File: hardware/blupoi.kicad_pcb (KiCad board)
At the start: 2 copper layers, 229.7 x 29.5 mm, 135 parts, among them P1 MICRO-B-USB, SW1 PM_BTN, U1 NRF52832, U2 TPS63031DSKR, U3 bno055, U4 ics43432, U5 BQ24075RGTT, U6 MAX16054AZT+T, U7 sip32408, X1 32MHz

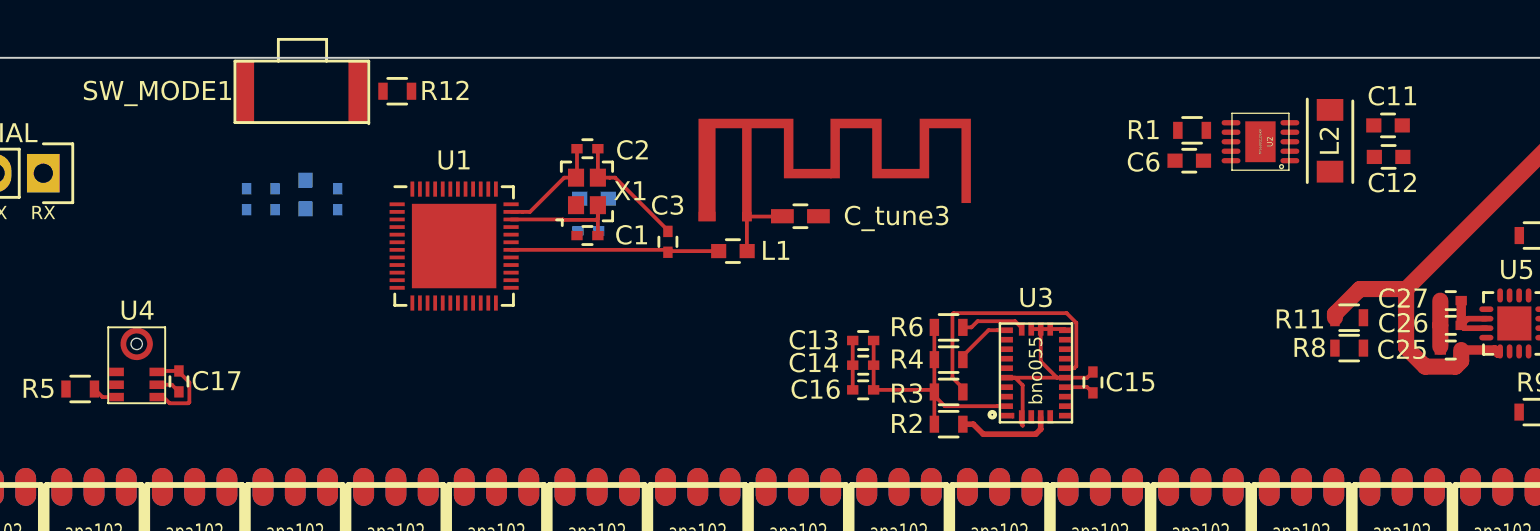
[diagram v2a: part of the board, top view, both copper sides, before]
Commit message: Change net name from VCHG to VREG
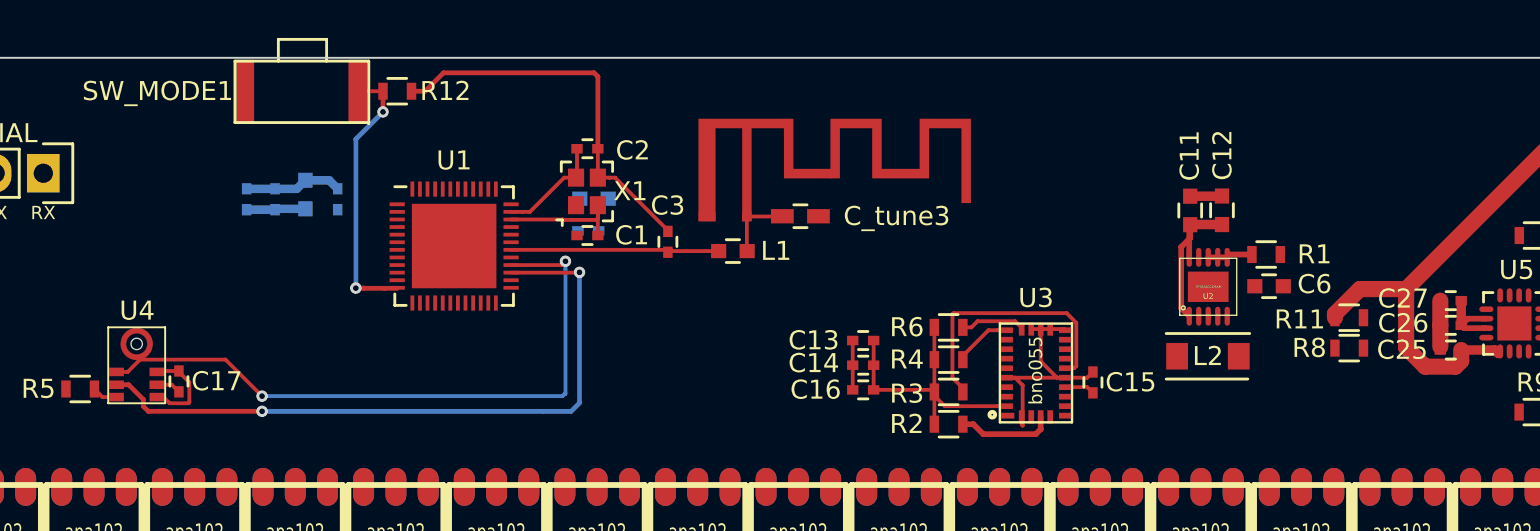
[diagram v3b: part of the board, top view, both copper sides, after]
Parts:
- moved L2 13.0 mm to (53.3, 108.8), turned to 180 degrees
- moved C11 11.3 mm to (52.4, 101.2), turned to 90 degrees
- moved C12 9.21 mm to (54.1, 101.2), turned to 90 degrees
- moved U2 8.12 mm to (53.4, 105.2), turned to 0 degrees
- moved C6 7.83 mm to (56.6, 105.2), turned to 180 degrees
- moved R1 7.61 mm to (56.4, 103.5), turned to 0 degrees
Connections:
- net VCHG renamed VREG
- U2 pad 2: Net-(U2-Pad2) -> Net-(L2-Pad2)
- U2 pad 4: Net-(U2-Pad4) -> Net-(L2-Pad1)
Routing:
- net MIC_I2S_SCK: track 0.00 -> 35.9 mm, vias 0 -> 2
- net MIC_I2S_WS: track 0.00 -> 34.7 mm, vias 0 -> 2
- net GND: track 78.9 -> 99.8 mm
- net Net-(R12-Pad1): track 0.00 -> 14.5 mm, vias 0 -> 2
- net V3.3: track 19.7 -> 31.4 mm
- net Net-(R1-Pad1): track 0.00 -> 2.36 mm

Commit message: Fixed SIP32408 footprint pins/pads lacking GND
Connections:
- U7 pad 2: Net-(U7-Pad2) -> GND
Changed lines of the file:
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@@
 (kicad_pcb (version 20170123) (host pcbnew no-vcs-found-7663~57~ubuntu16.10.1)
   (general
-    (links 514)
-    (no_connects 414)
+    (links 515)
+    (no_connects 415)
     (area -60.860001 93.069999 168.980001 122.650001)
     (thickness 1.6)
@@
     (zones 0)
     (modules 135)
-    (nets 233)
+    (nets 232)
   )
   (page A4)
@@
   (net 228 "Net-(U6-Pad5)")
   (net 229 "Net-(U1-Pad11)")
-  (net 230 "Net-(U7-Pad2)")
-  (net 231 "Net-(R12-Pad1)")
-  (net 232 VREG)
+  (net 230 "Net-(R12-Pad1)")
+  (net 231 VREG)
   (net_class Default "This is the default net class."
     (clearance 0.2)
@@
     (add_net "Net-(U6-Pad4)")
     (add_net "Net-(U6-Pad5)")
-    (add_net "Net-(U7-Pad2)")
     (add_net PM_!CHG)
     (add_net PM_!GOOD)
@@
     (add_net VUSB)
   )
+  (module sip32408:sip32408 (layer F.Cu)
+    (at 81.22 107.89 270)
+    (fp_text reference U7 (at -2.065 0.915) (layer F.SilkS)
+      (effects (font (size 1 1) (thickness 0.15)))
+    )
+    (fp_text value sip32408 (at 0 -2.54 270) (layer F.Fab)
+      (effects (font (size 1 1) (thickness 0.15)))
+    )
+    (fp_text user . (at 0.23 1.5 270) (layer F.SilkS)
+      (effects (font (size 1 1) (thickness 0.15)))
+    )
+    (fp_line (start -1.27 1.65) (end -1.27 0) (layer F.SilkS) (width 0.15))
+    (fp_line (start -0.02 1.65) (end -1.27 1.65) (layer F.SilkS) (width 0.15))
+    (fp_line (start -0.02 0) (end -0.02 1.65) (layer F.SilkS) (width 0.15))
+    (fp_line (start -1.27 0) (end -0.02 0) (layer F.SilkS) (width 0.15))
+    (pad 5 smd rect (at -0.645 0.825 270) (size 0.86 0.5) (layers F.Cu F.Paste F.Mask)
+      (net 2 GND))
+    (pad 3 smd rect (at -0.895 0 270) (size 0.3 0.7) (layers F.Cu F.Paste F.Mask)
+      (net 228 "Net-(U6-Pad5)"))
+    (pad 4 smd rect (at -0.395 0 270) (size 0.3 0.7) (layers F.Cu F.Paste F.Mask)
+      (net 184 VIN))
+    (pad 1 smd rect (at -0.395 1.65 270) (size 0.3 0.7) (layers F.Cu F.Paste F.Mask)
+      (net 231 VREG))
+    (pad 2 smd rect (at -0.895 1.65 270) (size 0.3 0.7) (layers F.Cu F.Paste F.Mask)
+      (net 2 GND))
+  )
   (module bno055:bno055 (layer F.Cu)
     (at 44.282 109.718 90)
@@
       (net 229 "Net-(U1-Pad11)"))
     (pad 12 smd rect (at -3 2.2) (size 0.8 0.2) (layers F.Cu F.Paste F.Mask)
-      (net 231 "Net-(R12-Pad1)") (clearance 0.001))
+      (net 230 "Net-(R12-Pad1)") (clearance 0.001))
     (pad 13 smd rect (at -2.2 3 90) (size 0.8 0.2) (layers F.Cu F.Paste F.Mask)
       (net 186 V3.3))
@@
     (fp_line (start -0.25 0.475) (end 0.25 0.475) (layer F.SilkS) (width 0.15))
     (pad 1 smd rect (at -0.55 0 180) (size 0.6 0.5) (layers F.Cu F.Paste F.Mask)
-      (net 232 VREG))
+      (net 231 VREG))
     (pad 2 smd rect (at 0.55 0 180) (size 0.6 0.5) (layers F.Cu F.Paste F.Mask)
       (net 2 GND))
@@
     (fp_line (start -0.25 0.475) (end 0.25 0.475) (layer F.SilkS) (width 0.15))
     (pad 1 smd rect (at -0.55 0 180) (size 0.6 0.5) (layers F.Cu F.Paste F.Mask)
-      (net 232 VREG))
+      (net 231 VREG))
     (pad 2 smd rect (at 0.55 0 180) (size 0.6 0.5) (layers F.Cu F.Paste F.Mask)
       (net 2 GND))
@@
       (net 201 PM_!CHG))
     (pad 10 smd oval (at 1.475 0.25 180) (size 0.75 0.3) (layers F.Cu F.Paste F.Mask)
-      (net 232 VREG))
+      (net 231 VREG))
     (pad 11 smd oval (at 1.475 -0.25 180) (size 0.75 0.3) (layers F.Cu F.Paste F.Mask)
-      (net 232 VREG))
+      (net 231 VREG))
     (pad 12 smd oval (at 1.475 -0.75 180) (size 0.75 0.3) (layers F.Cu F.Paste F.Mask)
       (net 188 "Net-(R8-Pad1)"))
@@
     )
   )
-  (module sip32408:sip32408 (layer F.Cu)
-    (at 81.22 107.89 270)
-    (fp_text reference U7 (at -2.065 0.915) (layer F.SilkS)
-      (effects (font (size 1 1) (thickness 0.15)))
-    )
-    (fp_text value sip32408 (at 0 -2.54 270) (layer F.Fab)
-      (effects (font (size 1 1) (thickness 0.15)))
-    )
-    (fp_line (start -1.27 0) (end -0.02 0) (layer F.SilkS) (width 0.15))
-    (fp_line (start -0.02 0) (end -0.02 1.65) (layer F.SilkS) (width 0.15))
-    (fp_line (start -0.02 1.65) (end -1.27 1.65) (layer F.SilkS) (width 0.15))
-    (fp_line (start -1.27 1.65) (end -1.27 0) (layer F.SilkS) (width 0.15))
-    (fp_text user . (at 0.23 1.5 270) (layer F.SilkS)
-      (effects (font (size 1 1) (thickness 0.15)))
-    )
-    (pad 2 smd rect (at -0.895 1.65 270) (size 0.3 0.7) (layers F.Cu F.Paste F.Mask)
-      (net 230 "Net-(U7-Pad2)"))
-    (pad 1 smd rect (at -0.395 1.65 270) (size 0.3 0.7) (layers F.Cu F.Paste F.Mask)
-      (net 232 VREG))
-    (pad 4 smd rect (at -0.395 0 270) (size 0.3 0.7) (layers F.Cu F.Paste F.Mask)
-      (net 184 VIN))
-    (pad 3 smd rect (at -0.895 0 270) (size 0.3 0.7) (layers F.Cu F.Paste F.Mask)
-      (net 228 "Net-(U6-Pad5)"))
-    (pad 1 smd rect (at -0.645 0.825 270) (size 0.86 0.5) (layers F.Cu F.Paste F.Mask)
-      (net 232 VREG))
-    (model ${KISYS3DMOD}/Housings_DFN_QFN.3dshapes/DFN-6-1EP_2x2mm_Pitch0.5mm.wrl
-      (at (xyz -0.02362204724409449 -0.03149606299212599 0))
-      (scale (xyz 0.75 0.75 0.75))
-      (rotate (xyz 0 0 90))
-    )
-  )
   (module Resistors_SMD:R_0603 (layer F.Cu)
     (at 10.64 94.88)
@@
       (net 2 GND))
     (pad 1 smd rect (at -0.75 0) (size 0.5 0.9) (layers F.Cu F.Paste F.Mask)
-      (net 231 "Net-(R12-Pad1)"))
+      (net 230 "Net-(R12-Pad1)"))
     (model Resistors_SMD.3dshapes/R_0603.wrl
       (at (xyz 0 0 0))
@@
     (fp_line (start 0 -0.0635) (end 0 3.2385) (layer F.SilkS) (width 0.15))
     (pad 1 smd rect (at 0.5715 1.651 180) (size 1 3.3) (layers F.Cu F.Paste F.Mask)
-      (net 231 "Net-(R12-Pad1)"))
+      (net 230 "Net-(R12-Pad1)"))
     (pad 2 smd rect (at 6.5405 1.651 180) (size 1 3.3) (layers F.Cu F.Paste F.Mask)
       (net 186 V3.3))
@@
   (via (at 163 93.6) (size 0.6) (drill 0.3) (layers F.Cu B.Cu) (net 192))
   (segment (start -42.43 120.52) (end -42.43 120.07) (width 0.2) (layer B.Cu) (net 203))
-  (segment (start 8.46 105.25) (end 8.884264 105.25) (width 0.25) (layer F.Cu) (net 231))
-  (segment (start 8.884264 105.25) (end 8.893784 105.25952) (width 0.25) (layer F.Cu) (net 231))
-  (segment (start 8.893784 105.25952) (end 9.975999 105.25952) (width 0.25) (layer F.Cu) (net 231))
-  (segment (start 9.975999 105.25952) (end 10.636 105.25952) (width 0.25) (layer F.Cu) (net 231))
-  (via (at 8.46 105.25) (size 0.6) (drill 0.3) (layers F.Cu B.Cu) (net 231))
-  (segment (start 8.46 97.4) (end 8.46 105.25) (width 0.25) (layer B.Cu) (net 231))
-  (segment (start 9.89 95.97) (end 8.46 97.4) (width 0.25) (layer B.Cu) (net 231))
-  (segment (start 9.89 94.88) (end 9.89 95.97) (width 0.25) (layer F.Cu) (net 231))
-  (via (at 9.89 95.97) (size 0.6) (drill 0.3) (layers F.Cu B.Cu) (net 231))
-  (segment (start 8.57 94.88) (end 9.89 94.88) (width 0.2) (layer F.Cu) (net 231))
-  (segment (start 66.68 105.91) (end 66.68 107.21) (width 0.5) (layer F.Cu) (net 232))
-  (segment (start 68.005 106.86) (end 67.03 106.86) (width 0.3) (layer F.Cu) (net 232))
-  (segment (start 67.03 106.86) (end 66.68 107.21) (width 0.3) (layer F.Cu) (net 232))
-  (segment (start 68.005 107.36) (end 66.83 107.36) (width 0.3) (layer F.Cu) (net 232))
-  (segment (start 66.83 107.36) (end 66.68 107.21) (width 0.3) (layer F.Cu) (net 232))
+  (segment (start 8.46 105.25) (end 8.884264 105.25) (width 0.25) (layer F.Cu) (net 230))
+  (segment (start 8.884264 105.25) (end 8.893784 105.25952) (width 0.25) (layer F.Cu) (net 230))
+  (segment (start 8.893784 105.25952) (end 9.975999 105.25952) (width 0.25) (layer F.Cu) (net 230))
+  (segment (start 9.975999 105.25952) (end 10.636 105.25952) (width 0.25) (layer F.Cu) (net 230))
+  (via (at 8.46 105.25) (size 0.6) (drill 0.3) (layers F.Cu B.Cu) (net 230))
+  (segment (start 8.46 97.4) (end 8.46 105.25) (width 0.25) (layer B.Cu) (net 230))
+  (segment (start 9.89 95.97) (end 8.46 97.4) (width 0.25) (layer B.Cu) (net 230))
+  (segment (start 9.89 94.88) (end 9.89 95.97) (width 0.25) (layer F.Cu) (net 230))
+  (via (at 9.89 95.97) (size 0.6) (drill 0.3) (layers F.Cu B.Cu) (net 230))
+  (segment (start 8.57 94.88) (end 9.89 94.88) (width 0.2) (layer F.Cu) (net 230))
+  (segment (start 66.68 105.91) (end 66.68 107.21) (width 0.5) (layer F.Cu) (net 231))
+  (segment (start 68.005 106.86) (end 67.03 106.86) (width 0.3) (layer F.Cu) (net 231))
+  (segment (start 67.03 106.86) (end 66.68 107.21) (width 0.3) (layer F.Cu) (net 231))
+  (segment (start 68.005 107.36) (end 66.83 107.36) (width 0.3) (layer F.Cu) (net 231))
+  (segment (start 66.83 107.36) (end 66.68 107.21) (width 0.3) (layer F.Cu) (net 231))
   (zone (net 0) (net_name "") (layer F.Cu) (hatch edge 0.508)
     (connect_pads (clearance 0.508))

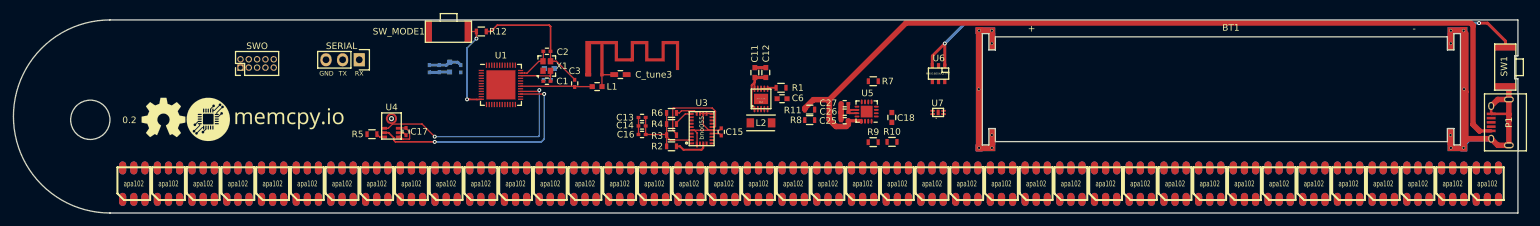
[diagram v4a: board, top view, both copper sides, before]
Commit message: Started routing v0.2
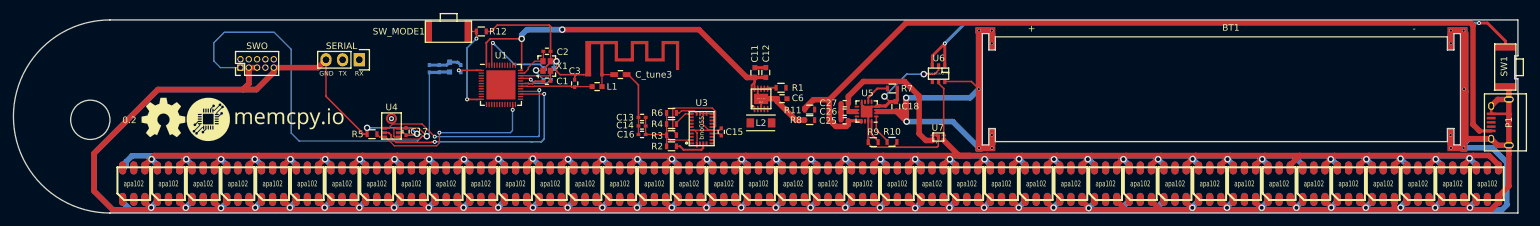
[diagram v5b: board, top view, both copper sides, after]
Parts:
- moved U7 3.76 mm to (81.2, 111.6)
- moved R7 3.12 mm to (73.4, 103.6)
- moved C18 1.78 mm to (73.9, 106.3), turned to 90 degrees
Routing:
- net GND: track 99.8 -> 946.7 mm, vias 0 -> 43
- net VIN: track 0.00 -> 613.4 mm, vias 0 -> 38
- net V3.3: track 31.4 -> 157.5 mm, vias 0 -> 3
- net VBAT: track 12.9 -> 61.4 mm, vias 0 -> 2
- net MIC_I2S_SD: track 1.33 -> 27.3 mm, vias 0 -> 2
- net VREG: track 4.16 -> 27.7 mm
- net Net-(C10-Pad1): track 0.00 -> 13.0 mm, vias 0 -> 1
- net Net-(U6-Pad5): track 0.00 -> 8.56 mm
- net Net-(C7-Pad1): track 0.00 -> 5.16 mm, vias 0 -> 1
- net Net-(R10-Pad1): track 0.00 -> 4.56 mm
- net PM_EN1: track 0.00 -> 4.17 mm
- net Net-(C4-Pad1): track 0.00 -> 3.87 mm, vias 0 -> 1
- net PM_ISET: track 0.00 -> 3.61 mm
- net Net-(C1-Pad1): track 6.90 -> 6.29 mm

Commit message: Started routing v0.2..
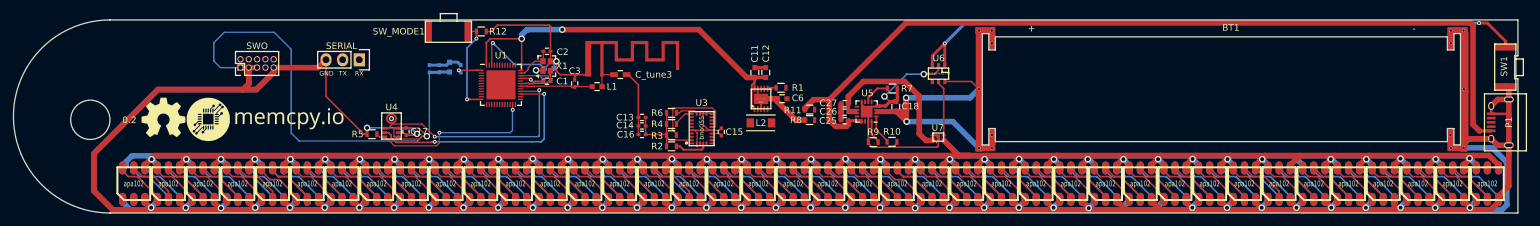
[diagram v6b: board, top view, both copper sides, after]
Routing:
- net Net-(LED0_4-Pad5): track 0.00 -> 8.02 mm
- net Net-(LED0_33-Pad5): track 0.00 -> 8.02 mm
- net Net-(LED0_16-Pad5): track 0.00 -> 8.02 mm
- net Net-(LED0_1-Pad5): track 0.00 -> 8.02 mm
- net Net-(LED1_39-Pad5): track 0.00 -> 7.82 mm
- net Net-(LED1_38-Pad5): track 0.00 -> 7.82 mm
- net Net-(LED1_36-Pad5): track 0.00 -> 7.82 mm
- net Net-(LED1_34-Pad5): track 0.00 -> 7.82 mm
- net Net-(LED1_31-Pad5): track 0.00 -> 7.82 mm
- net Net-(LED1_26-Pad5): track 0.00 -> 7.82 mm
- net Net-(LED0_38-Pad6): track 0.00 -> 7.82 mm
- net Net-(LED0_37-Pad6): track 0.00 -> 7.82 mm
- net Net-(LED0_35-Pad6): track 0.00 -> 7.82 mm
- net Net-(LED0_30-Pad6): track 0.00 -> 7.82 mm
- net Net-(LED0_25-Pad6): track 0.00 -> 7.82 mm
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
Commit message: Started routing v0.2...
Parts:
- moved SWO 38.8 mm to (11.2, 110.8)
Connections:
- LED1_1 pad 1: /apa102_1/SPI0_MOSI -> APA102_1_MOSI
- LED1_1 pad 2: /apa102_1/SPI0_SCK -> APA102_1_SCK
- U1 pad 10: Net-(U1-Pad10) -> MIC_I2S_SD
- U1 pad 23: MIC_I2S_SD -> Net-(U1-Pad23)
- U1 pad 27: MIC_I2S_SCK -> ACC_I2C_SCL
- U1 pad 28: MIC_I2S_WS -> ACC_I2C_SDA
- U1 pad 37: APA102_0_MOSI -> Net-(U1-Pad37)
- U1 pad 38: APA102_0_SCK -> Net-(U1-Pad38)
- U1 pad 39: APA102_1_MOSI -> Net-(U1-Pad39)
- U1 pad 4: Net-(U1-Pad4) -> APA102_0_SCK
- U1 pad 40: APA102_1_SCK -> Net-(U1-Pad40)
- U1 pad 5: Net-(U1-Pad5) -> APA102_0_MOSI
- U1 pad 6: Net-(U1-Pad6) -> APA102_1_SCK
- U1 pad 7: Net-(U1-Pad7) -> APA102_1_MOSI
- U1 pad 8: ACC_I2C_SCL -> MIC_I2S_WS
- U1 pad 9: ACC_I2C_SDA -> MIC_I2S_SCK
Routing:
- net APA102_0_SCK: track 0.00 -> 72.8 mm, vias 0 -> 2
- net APA102_0_MOSI: track 0.00 -> 72.8 mm, vias 0 -> 2
- net APA102_1_SCK: track 0.00 -> 70.7 mm, vias 0 -> 1
- net APA102_1_MOSI: track 0.00 -> 70.0 mm, vias 0 -> 1
- net V3.3: track 157.5 -> 123.1 mm, vias 3 -> 4
- net TX: track 0.00 -> 22.2 mm
- net RX: track 0.00 -> 19.5 mm
- net GND: track 946.7 -> 965.8 mm
- net VIN: track 613.4 -> 628.7 mm, vias 38 -> 40
- net MIC_I2S_SCK: track 35.9 -> 21.6 mm
- net MIC_I2S_WS: track 34.7 -> 21.7 mm
- net SWDIO: track 0.00 -> 11.5 mm, vias 0 -> 1
- net SWCLK: track 0.00 -> 9.48 mm, vias 0 -> 1
- net MIC_I2S_SD: track 27.3 -> 23.1 mm
- net SWO: track 0.00 -> 3.87 mm
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
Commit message: Finished routing for v0.2
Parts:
- moved SWO 1.37 mm to (11.1, 112.2)
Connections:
- U1 pad 15: PM_EN1 -> PM_!CHG
- U1 pad 16: PM_EN2 -> PM_!GOOD
- U1 pad 17: PM_!GOOD -> PM_EN1
- U1 pad 18: PM_!CHG -> PM_EN2
- U1 pad 27: ACC_I2C_SCL -> ACC_I2C_SDA
- U1 pad 28: ACC_I2C_SDA -> ACC_I2C_SCL
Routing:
- net GND: track 965.8 -> 1107.7 mm, vias 43 -> 54
- net PM_SWITCH: track 96.6 -> 166.1 mm, vias 2 -> 4
- net PM_EN2: track 0.00 -> 68.1 mm, vias 0 -> 4
- net PM_ISET: track 3.61 -> 70.2 mm, vias 0 -> 2
- net PM_!CHG: track 0.00 -> 64.9 mm, vias 0 -> 2
- net PM_!GOOD: track 0.00 -> 64.8 mm, vias 0 -> 2
- net PM_EN1: track 4.17 -> 68.5 mm, vias 0 -> 2
- net V3.3: track 123.1 -> 153.0 mm, vias 4 -> 9
- net ACC_I2C_SDA: track 5.07 -> 29.6 mm, vias 1 -> 0
- net ACC_I2C_SCL: track 5.64 -> 29.0 mm, vias 1 -> 0
- net Net-(R8-Pad1): track 0.00 -> 10.2 mm, vias 0 -> 2
- net Net-(R3-Pad1): track 14.0 -> 9.31 mm, vias 0 -> 2
- net SWDIO: track 11.5 -> 14.8 mm
- net VUSB: track 136.0 -> 137.6 mm
- net SWO: track 3.87 -> 5.32 mm
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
